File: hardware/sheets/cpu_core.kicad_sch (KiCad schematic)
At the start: 32 parts, among them U1 V20, U10 74HCT32, U11 74HCT125, U12 74HCT157, U13 74HCT04, U14 TCM809, U2 74HCT573, U3 74HCT573, U4 74HCT573, U5 74HCT245, U6 74HCT138, U7 74HCT00, U8 74HCT74, U9 74HCT163

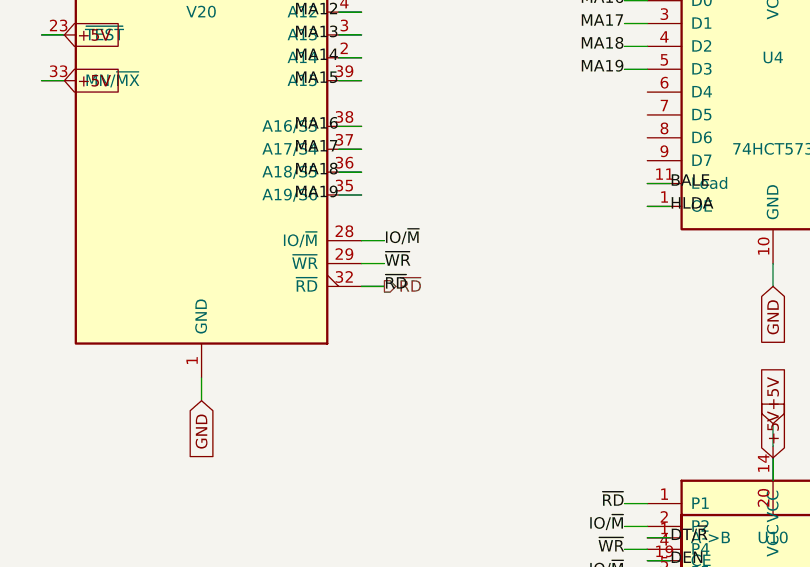
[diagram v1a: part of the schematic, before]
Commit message: Fix all low-severity + toolchain design-review findings
Low:
- LPT IRQ7 via tri-state '125 (NAND-enabled ack pulse) - shareable line
- card_com JP2 IRQ strap follows the base-address strap (was IRQ4-only)
- Supervisor USB-A VBUS fused (500mA polyfuse)
- card_isatest: DUT_PWR_EN moved to the control '595 (addr shifts can't
  glitch DUT power); '165s -> 74HC grade (HCT needs VCC 4.5-5.5V)
- /3 duty comments corrected; U13 marked load-bearing inverting buffer
- RTC AS hold-path bench note; duplicate ~RD stub removed
- mxbus PRIV_DECODE emptied (Y5 never leaves cpu_core)

Toolchain:
- build.py/build_cards return real exit codes, failing on structural ERC
  (endpoint_off_grid/unconnected_wire_endpoint/multiple_net_names) or a
  failed netlist export
- KiCad paths resolved via mxsch.kicad_cli()/kicad_symdir() (env, PATH,
  snap `current`) - no pinned snap revision anywhere
- Deterministic UUIDs (uuid5 title-seed + counter): rebuilds are
  byte-identical (verified); this rewrites every UUID once
- S-expression string escapes now round-trip (parse decodes, dump encodes)
- CLAUDE.md updated to match

The new structural gate immediately caught its own batch's bug (pull row
placed inside card_isatest's J2 pin field) - moved and re-verified.

Co-Authored-By: Claude Fable 5 <noreply@anthropic.com>
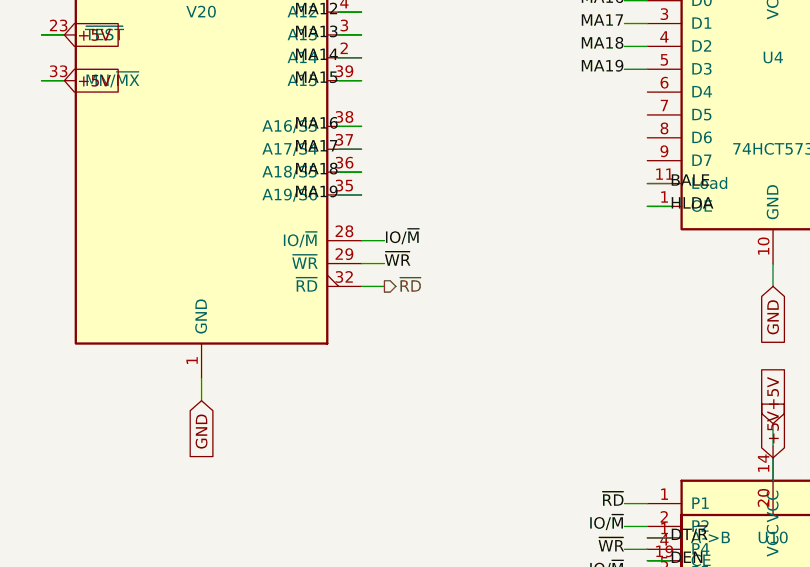
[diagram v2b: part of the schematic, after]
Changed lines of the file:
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@@
 	(wire
 		(pts
-			(xy 119.38 187.96)
-			(xy 121.92 187.96)
-		)
-		(stroke
-			(width 0)
-			(type default)
-		)
-	)
-	(label "~{RD}"
-		(at 121.92 187.96 0)
-		(effects
-			(font
-				(size 1.27 1.27)
-			)
-		)
-	)
-	(wire
-		(pts
 			(xy 119.38 185.42)
 			(xy 121.92 185.42)
@@
 		(instances
 			(project "mini-xt"
-				(path "/9d1a32b9-fdc3-4ebf-878d-e57919a1b88e/ead79a1c-d771-4618-8d33-c03035d0f824"
+				(path "/26736c46-8b40-5460-874f-03596d17270c/36a61212-e622-5b01-8e81-aba0acbc9887"
 					(reference "U101")
 					(unit 1)
@@
 		(instances
 			(project "mini-xt"
-				(path "/9d1a32b9-fdc3-4ebf-878d-e57919a1b88e/ead79a1c-d771-4618-8d33-c03035d0f824"
+				(path "/26736c46-8b40-5460-874f-03596d17270c/36a61212-e622-5b01-8e81-aba0acbc9887"
 					(reference "U110")
 					(unit 1)
@@
 		(instances
 			(project "mini-xt"
-				(path "/9d1a32b9-fdc3-4ebf-878d-e57919a1b88e/ead79a1c-d771-4618-8d33-c03035d0f824"
+				(path "/26736c46-8b40-5460-874f-03596d17270c/36a61212-e622-5b01-8e81-aba0acbc9887"
 					(reference "U111")
 					(unit 1)
@@
 		(instances
 			(project "mini-xt"
-				(path "/9d1a32b9-fdc3-4ebf-878d-e57919a1b88e/ead79a1c-d771-4618-8d33-c03035d0f824"
+				(path "/26736c46-8b40-5460-874f-03596d17270c/36a61212-e622-5b01-8e81-aba0acbc9887"
 					(reference "U102")
 					(unit 1)
@@
 		(instances
 			(project "mini-xt"
-				(path "/9d1a32b9-fdc3-4ebf-878d-e57919a1b88e/ead79a1c-d771-4618-8d33-c03035d0f824"
+				(path "/26736c46-8b40-5460-874f-03596d17270c/36a61212-e622-5b01-8e81-aba0acbc9887"
 					(reference "U103")
 					(unit 1)
@@
 		(instances
 			(project "mini-xt"
-				(path "/9d1a32b9-fdc3-4ebf-878d-e57919a1b88e/ead79a1c-d771-4618-8d33-c03035d0f824"
+				(path "/26736c46-8b40-5460-874f-03596d17270c/36a61212-e622-5b01-8e81-aba0acbc9887"
 					(reference "U104")
 					(unit 1)
@@
 		(instances
 			(project "mini-xt"
-				(path "/9d1a32b9-fdc3-4ebf-878d-e57919a1b88e/ead79a1c-d771-4618-8d33-c03035d0f824"
+				(path "/26736c46-8b40-5460-874f-03596d17270c/36a61212-e622-5b01-8e81-aba0acbc9887"
 					(reference "U105")
 					(unit 1)
@@
 		(instances
 			(project "mini-xt"
-				(path "/9d1a32b9-fdc3-4ebf-878d-e57919a1b88e/ead79a1c-d771-4618-8d33-c03035d0f824"
+				(path "/26736c46-8b40-5460-874f-03596d17270c/36a61212-e622-5b01-8e81-aba0acbc9887"
 					(reference "U106")
 					(unit 1)
@@
 		(instances
 			(project "mini-xt"
-				(path "/9d1a32b9-fdc3-4ebf-878d-e57919a1b88e/ead79a1c-d771-4618-8d33-c03035d0f824"
+				(path "/26736c46-8b40-5460-874f-03596d17270c/36a61212-e622-5b01-8e81-aba0acbc9887"
 					(reference "U107")
 					(unit 1)
@@
 		(instances
 			(project "mini-xt"
-				(path "/9d1a32b9-fdc3-4ebf-878d-e57919a1b88e/ead79a1c-d771-4618-8d33-c03035d0f824"
+				(path "/26736c46-8b40-5460-874f-03596d17270c/36a61212-e622-5b01-8e81-aba0acbc9887"
 					(reference "RAM101")
 					(unit 1)
@@
 		(instances
 			(project "mini-xt"
-				(path "/9d1a32b9-fdc3-4ebf-878d-e57919a1b88e/ead79a1c-d771-4618-8d33-c03035d0f824"
+				(path "/26736c46-8b40-5460-874f-03596d17270c/36a61212-e622-5b01-8e81-aba0acbc9887"
 					(reference "RAM102")
 					(unit 1)
@@
 		(instances
 			(project "mini-xt"
-				(path "/9d1a32b9-fdc3-4ebf-878d-e57919a1b88e/ead79a1c-d771-4618-8d33-c03035d0f824"
+				(path "/26736c46-8b40-5460-874f-03596d17270c/36a61212-e622-5b01-8e81-aba0acbc9887"
 					(reference "OSC101")
 					(unit 1)
@@
 		(instances
 			(project "mini-xt"
-				(path "/9d1a32b9-fdc3-4ebf-878d-e57919a1b88e/ead79a1c-d771-4618-8d33-c03035d0f824"
+				(path "/26736c46-8b40-5460-874f-03596d17270c/36a61212-e622-5b01-8e81-aba0acbc9887"
 					(reference "U108")
 					(unit 1)
@@
 		(instances
 			(project "mini-xt"
-				(path "/9d1a32b9-fdc3-4ebf-878d-e57919a1b88e/ead79a1c-d771-4618-8d33-c03035d0f824"
+				(path "/26736c46-8b40-5460-874f-03596d17270c/36a61212-e622-5b01-8e81-aba0acbc9887"
 					(reference "U109")
 					(unit 1)
@@
 		(instances
 			(project "mini-xt"
-				(path "/9d1a32b9-fdc3-4ebf-878d-e57919a1b88e/ead79a1c-d771-4618-8d33-c03035d0f824"
+				(path "/26736c46-8b40-5460-874f-03596d17270c/36a61212-e622-5b01-8e81-aba0acbc9887"
 					(reference "U112")
 					(unit 1)
@@
 		(instances
 			(project "mini-xt"
-				(path "/9d1a32b9-fdc3-4ebf-878d-e57919a1b88e/ead79a1c-d771-4618-8d33-c03035d0f824"
+				(path "/26736c46-8b40-5460-874f-03596d17270c/36a61212-e622-5b01-8e81-aba0acbc9887"
 					(reference "U113")
 					(unit 1)
@@
 		(instances
 			(project "mini-xt"
-				(path "/9d1a32b9-fdc3-4ebf-878d-e57919a1b88e/ead79a1c-d771-4618-8d33-c03035d0f824"
+				(path "/26736c46-8b40-5460-874f-03596d17270c/36a61212-e622-5b01-8e81-aba0acbc9887"
 					(reference "U114")
 					(unit 1)
@@
 		(instances
 			(project "mini-xt"
-				(path "/9d1a32b9-fdc3-4ebf-878d-e57919a1b88e/ead79a1c-d771-4618-8d33-c03035d0f824"
+				(path "/26736c46-8b40-5460-874f-03596d17270c/36a61212-e622-5b01-8e81-aba0acbc9887"
 					(reference "R101")
 					(unit 1)
@@
 		(instances
 			(project "mini-xt"
-				(path "/9d1a32b9-fdc3-4ebf-878d-e57919a1b88e/ead79a1c-d771-4618-8d33-c03035d0f824"
+				(path "/26736c46-8b40-5460-874f-03596d17270c/36a61212-e622-5b01-8e81-aba0acbc9887"
 					(reference "R102")
 					(unit 1)
@@
 		(instances
 			(project "mini-xt"
-				(path "/9d1a32b9-fdc3-4ebf-878d-e57919a1b88e/ead79a1c-d771-4618-8d33-c03035d0f824"
+				(path "/26736c46-8b40-5460-874f-03596d17270c/36a61212-e622-5b01-8e81-aba0acbc9887"
 					(reference "R103")
 					(unit 1)
@@
 		(instances
 			(project "mini-xt"
-				(path "/9d1a32b9-fdc3-4ebf-878d-e57919a1b88e/ead79a1c-d771-4618-8d33-c03035d0f824"
+				(path "/26736c46-8b40-5460-874f-03596d17270c/36a61212-e622-5b01-8e81-aba0acbc9887"
 					(reference "R104")
 					(unit 1)
@@
 		(instances
 			(project "mini-xt"
-				(path "/9d1a32b9-fdc3-4ebf-878d-e57919a1b88e/ead79a1c-d771-4618-8d33-c03035d0f824"
+				(path "/26736c46-8b40-5460-874f-03596d17270c/36a61212-e622-5b01-8e81-aba0acbc9887"
 					(reference "R105")
 					(unit 1)
@@
 		(instances
 			(project "mini-xt"
-				(path "/9d1a32b9-fdc3-4ebf-878d-e57919a1b88e/ead79a1c-d771-4618-8d33-c03035d0f824"
+				(path "/26736c46-8b40-5460-874f-03596d17270c/36a61212-e622-5b01-8e81-aba0acbc9887"
 					(reference "R106")
 					(unit 1)
@@
 		(instances
 			(project "mini-xt"
-				(path "/9d1a32b9-fdc3-4ebf-878d-e57919a1b88e/ead79a1c-d771-4618-8d33-c03035d0f824"
+				(path "/26736c46-8b40-5460-874f-03596d17270c/36a61212-e622-5b01-8e81-aba0acbc9887"
 					(reference "R107")
 					(unit 1)
@@
 		(instances
 			(project "mini-xt"
-				(path "/9d1a32b9-fdc3-4ebf-878d-e57919a1b88e/ead79a1c-d771-4618-8d33-c03035d0f824"
+				(path "/26736c46-8b40-5460-874f-03596d17270c/36a61212-e622-5b01-8e81-aba0acbc9887"
 					(reference "R108")
 					(unit 1)
@@
 		(instances
 			(project "mini-xt"
-				(path "/9d1a32b9-fdc3-4ebf-878d-e57919a1b88e/ead79a1c-d771-4618-8d33-c03035d0f824"
+				(path "/26736c46-8b40-5460-874f-03596d17270c/36a61212-e622-5b01-8e81-aba0acbc9887"
 					(reference "C110")
 					(unit 1)
@@
 		(instances
 			(project "mini-xt"
-				(path "/9d1a32b9-fdc3-4ebf-878d-e57919a1b88e/ead79a1c-d771-4618-8d33-c03035d0f824"
+				(path "/26736c46-8b40-5460-874f-03596d17270c/36a61212-e622-5b01-8e81-aba0acbc9887"
 					(reference "C111")
 					(unit 1)
@@
 		(instances
 			(project "mini-xt"
-				(path "/9d1a32b9-fdc3-4ebf-878d-e57919a1b88e/ead79a1c-d771-4618-8d33-c03035d0f824"
+				(path "/26736c46-8b40-5460-874f-03596d17270c/36a61212-e622-5b01-8e81-aba0acbc9887"
 					(reference "C112")
 					(unit 1)
@@
 		(instances
 			(project "mini-xt"
-				(path "/9d1a32b9-fdc3-4ebf-878d-e57919a1b88e/ead79a1c-d771-4618-8d33-c03035d0f824"
+				(path "/26736c46-8b40-5460-874f-03596d17270c/36a61212-e622-5b01-8e81-aba0acbc9887"
 					(reference "C113")
 					(unit 1)
@@
 		(instances
 			(project "mini-xt"
-				(path "/9d1a32b9-fdc3-4ebf-878d-e57919a1b88e/ead79a1c-d771-4618-8d33-c03035d0f824"
+				(path "/26736c46-8b40-5460-874f-03596d17270c/36a61212-e622-5b01-8e81-aba0acbc9887"
 					(reference "C114")
 					(unit 1)
@@
 		(instances
 			(project "mini-xt"
-				(path "/9d1a32b9-fdc3-4ebf-878d-e57919a1b88e/ead79a1c-d771-4618-8d33-c03035d0f824"
+				(path "/26736c46-8b40-5460-874f-03596d17270c/36a61212-e622-5b01-8e81-aba0acbc9887"
 					(reference "C115")
 					(unit 1)
@@
 		(instances
 			(project "mini-xt"
-				(path "/9d1a32b9-fdc3-4ebf-878d-e57919a1b88e/ead79a1c-d771-4618-8d33-c03035d0f824"
+				(path "/26736c46-8b40-5460-874f-03596d17270c/36a61212-e622-5b01-8e81-aba0acbc9887"
 					(reference "C116")
 					(unit 1)

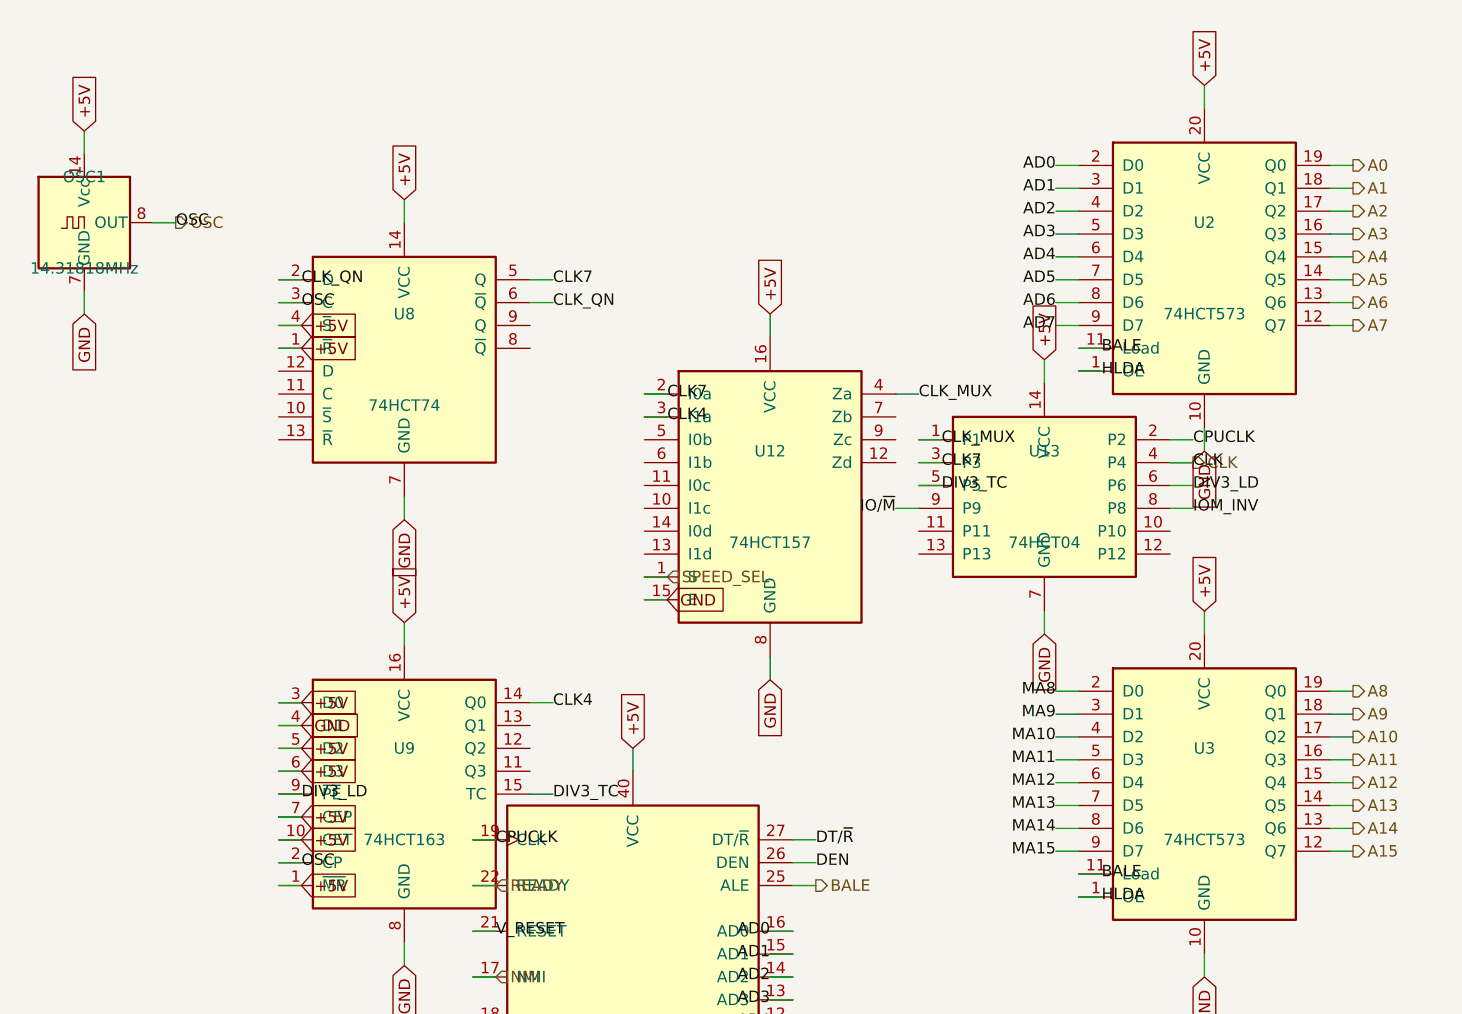
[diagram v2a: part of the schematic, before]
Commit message: JLCPCB sourcing pass: verify pinouts, LCSC part numbers, SMD build
Custom-symbol verification (open-questions Q5 resolved):
- MAX3241 symbol was wrong on nearly every pin and used MAX3243-style
  control names; regenerated to the real SSOP-28 pinout (SHDN#/EN#/
  R1OUTB/R2OUTB) and com_port rewired -- EN# must be GROUNDED (the old
  ~FORCEON-high would have disabled the receivers on real silicon)
- DS12C887 symbol wrong on 4 pins (DS=17, RESET#=18, IRQ#=19, SQW=23)

Sourcing (every part checked against the JLC DB; ~45 line items):
- New tools/parts.py maps (lib_id, value) -> LCSC; build.py applies it as
  an 'LCSC Part Num' property on every component (384 across the project)
- Sheets stay generic; stock-forced substitutions bound in the map:
  '374->'574 (parallel rewired), '163->'161, '157->HC157 (+HCT-buffered
  3.3V selects, I0/I1 swapped), '02->HC02, TCM809->MCP809, 2N3904->MMBT3904
- bus_mcu address counters moved to the 3.3V domain (HC161 on 3V3_BUS,
  loaded from MCU-side MD0-7; HCT244s read the 3.3V outputs at TTL Vih)
- 14.318 XOs are 3.3V-only parts: powered from 3V3, squared up via spare
  HCT gates (cpu_core U13, card_isatest U19)
- COM baud reference is now a 1.8432MHz crystal on the 16C550's XIN/XOUT
  (3.3V-only oscillators vs a 5V-only soft card)
- Supervisor QSPI header replaced with a real W25Q128JVSIQ
- Socket policy (fab installs sockets): V20 DIP-40, SRAM DIP-32 (no 5V
  512Kx8 SRAM at JLC at all), DS12C887 DIP-24, female headers for modules

Docs: CLAUDE.md fabrication-constraints section (SMD, 100x100mm, generic-
symbols rule, voltage-domain rule); README + hardware/README fab notes;
notes/jlcpcb-sourcing.md (decisions, thin-stock flags, not-at-JLC list);
stale questions-sidecar.md collapsed to its supersession record.

Rebuilt motherboard + cards: structural ERC 0, byte-identical rebuilds.

Co-Authored-By: Claude Fable 5 <noreply@anthropic.com>
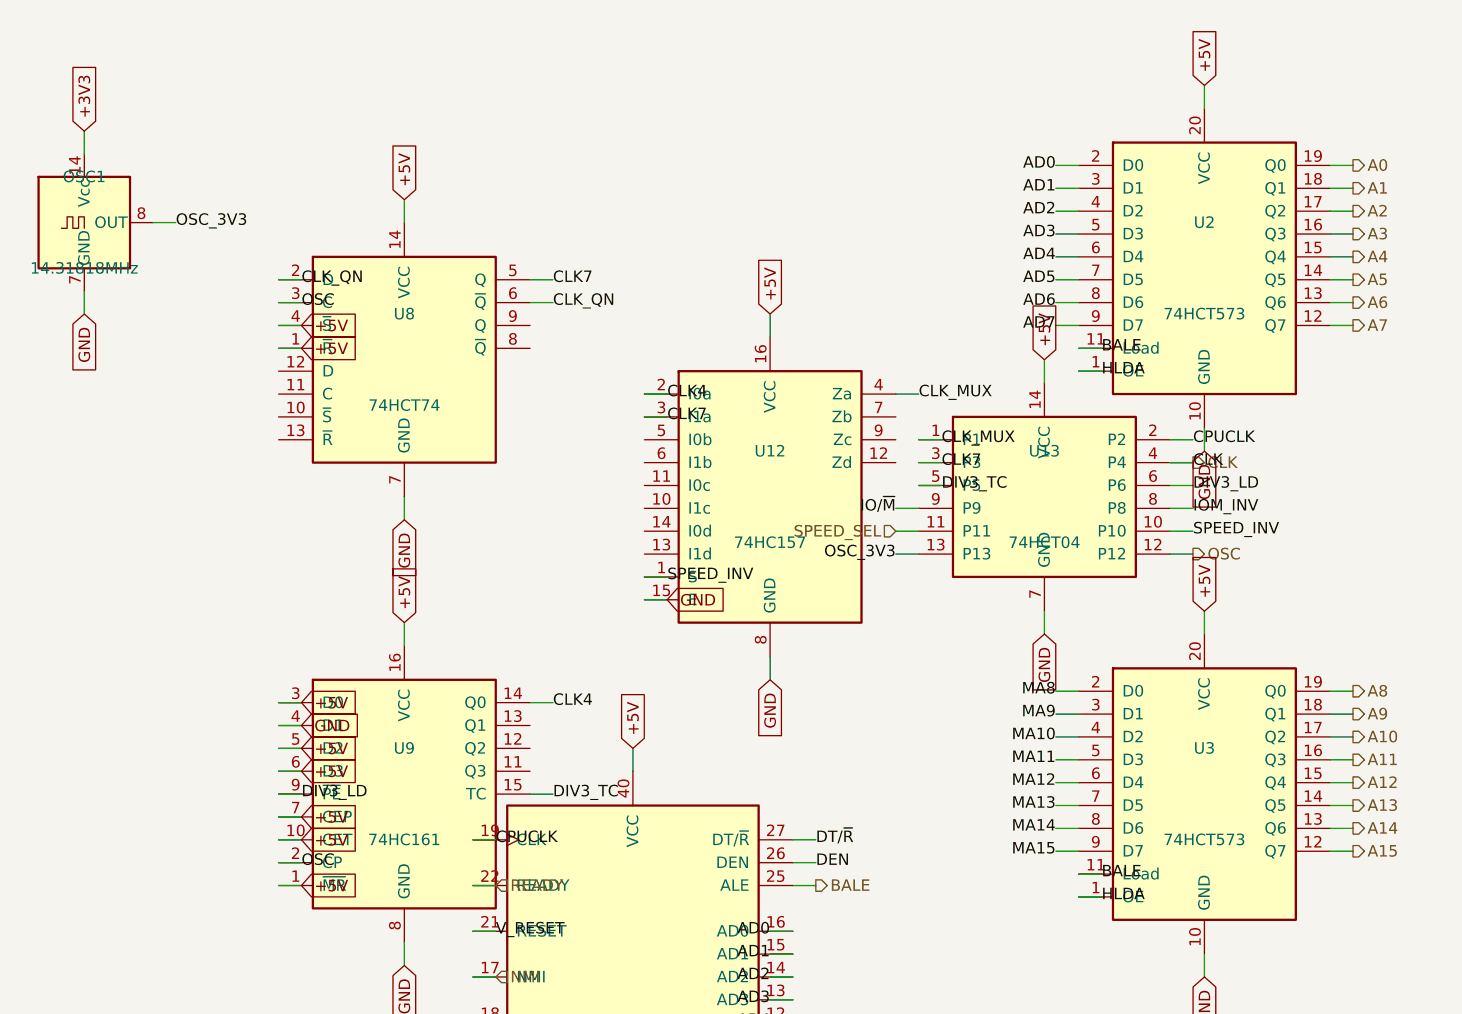
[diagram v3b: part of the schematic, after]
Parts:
- C10, C11, C12, C13, C14, C15, C16: LCSC Part Num (none) -> C14663
- OSC1: LCSC Part Num (none) -> C49330311
- R1, R2, R3, R4, R5, R6, R7, R8: LCSC Part Num (none) -> C25804
- RAM1, RAM2: LCSC Part Num (none) -> C72122
- U1: LCSC Part Num (none) -> C2332
- U10: LCSC Part Num (none) -> C5985
- U11: LCSC Part Num (none) -> C5962
- U12: value 74HCT157 -> 74HC157; LCSC Part Num (none) -> C5609
- U13: LCSC Part Num (none) -> C672096
- U14: LCSC Part Num (none) -> C511285
- U2, U3, U4: LCSC Part Num (none) -> C5209384
- U5: LCSC Part Num (none) -> C5979
- U6: LCSC Part Num (none) -> C5965
- U7: LCSC Part Num (none) -> C282337
- U8: LCSC Part Num (none) -> C686657
- U9: value 74HCT163 -> 74HC161; LCSC Part Num (none) -> C5610
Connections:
- net +5V: no longer OSC1.14 (Vcc)
- net CLK4: now also U12.2 (I0a); no longer U12.3 (I1a)
- net CLK7: now also U12.3 (I1a); no longer U12.2 (I0a)
- net OSC: now also U13.12 (P12); no longer OSC1.8 (OUT)
- net SPEED_SEL: now also U13.11 (P11); no longer U12.1 (S)
- net SPEED_INV: now reaches U13.10 (P10)
- net SPEED_INV: now also U12.1 (S)
- net OSC_3V3: now reaches U13.13 (P13)
- net OSC_3V3: now also OSC1.8 (OUT)
- new net +3V3: OSC1.14 (Vcc)

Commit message: Swap DIP sockets to machined-pin versions
V20 DIP-40 -> C2874018, SRAM DIP-32 x2 -> C2874017, DS12C887 DIP-24 ->
C2684765 (all round-hole/machined, verified 600 mil row spacing).
Better grip and repeated-insertion tolerance for the vintage chips;
~$2.50/board-set over stamped tin. Stamped fallbacks noted in
jlcpcb-sourcing.md.

Co-Authored-By: Claude Fable 5 <noreply@anthropic.com>
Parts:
- RAM1, RAM2: LCSC Part Num C72122 -> C2874017
- U1: LCSC Part Num C2332 -> C2874018
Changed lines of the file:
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@@
 			)
 		)
-		(property "LCSC Part Num" "C2332"
+		(property "LCSC Part Num" "C2874018"
 			(at 101.6 152.4 0)
 			(effects
@@
 			)
 		)
-		(property "LCSC Part Num" "C72122"
+		(property "LCSC Part Num" "C2874017"
 			(at 302.26 76.2 0)
 			(effects
@@
 			)
 		)
-		(property "LCSC Part Num" "C72122"
+		(property "LCSC Part Num" "C2874017"
 			(at 302.26 175.26 0)
 			(effects
